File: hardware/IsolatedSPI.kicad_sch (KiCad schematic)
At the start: 9 parts, among them IC6 LTC6820IMS

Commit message: schematic done
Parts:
- removed D5: ESDA5V3SC5, Package_TO_SOT_SMD:SOT-23-6, symbol Power_Protection:ESDA5V3SC5
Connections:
- no-connect marks 2 -> 0
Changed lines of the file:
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@@
 	(paper "A4")
-	(junction
-		(at 170.18 83.82)
-		(diameter 0)
-		(color 0 0 0 0)
-	)
 	(junction
 		(at 95.25 111.76)
@@
 	)
 	(junction
-		(at 172.72 86.36)
-		(diameter 0)
-		(color 0 0 0 0)
-	)
-	(junction
 		(at 85.09 86.36)
 		(diameter 0)
@@
 		(color 0 0 0 0)
 	)
-	(no_connect
-		(at 175.26 81.28)
-	)
-	(no_connect
-		(at 167.64 81.28)
-	)
 	(wire
 		(pts
@@
 	(wire
 		(pts
-			(xy 120.65 86.36) (xy 172.72 86.36)
+			(xy 120.65 86.36) (xy 194.31 86.36)
 		)
 		(stroke
@@
 	(wire
 		(pts
-			(xy 172.72 81.28) (xy 172.72 86.36)
-		)
-		(stroke
-			(width 0)
-			(type default)
-		)
-	)
-	(wire
-		(pts
 			(xy 194.31 83.82) (xy 194.31 81.28)
 		)
@@
 	(wire
 		(pts
-			(xy 172.72 68.58) (xy 172.72 71.12)
-		)
-		(stroke
-			(width 0)
-			(type default)
-		)
-	)
-	(wire
-		(pts
 			(xy 129.54 116.84) (xy 120.65 116.84)
 		)
@@
 	(wire
 		(pts
-			(xy 170.18 83.82) (xy 194.31 83.82)
-		)
-		(stroke
-			(width 0)
-			(type default)
-		)
-	)
-	(wire
-		(pts
 			(xy 92.71 86.36) (xy 95.25 86.36)
 		)
@@
 	(wire
 		(pts
-			(xy 170.18 81.28) (xy 170.18 83.82)
-		)
-		(stroke
-			(width 0)
-			(type default)
-		)
-	)
-	(wire
-		(pts
 			(xy 85.09 86.36) (xy 87.63 86.36)
 		)
@@
 	(wire
 		(pts
-			(xy 172.72 86.36) (xy 194.31 86.36)
-		)
-		(stroke
-			(width 0)
-			(type default)
-		)
-	)
-	(wire
-		(pts
 			(xy 203.2 81.28) (xy 203.2 82.55)
 		)
@@
 	(wire
 		(pts
-			(xy 120.65 83.82) (xy 170.18 83.82)
+			(xy 120.65 83.82) (xy 194.31 83.82)
 		)
 		(stroke
@@
 					(unit 1)
 				)
-			)
-		)
-	)
-	(symbol
-		(lib_name "GND_31")
-		(lib_id "power:GND")
-		(at 172.72 68.58 180)
-		(unit 1)
-		(exclude_from_sim no)
-		(in_bom yes)
-		(on_board yes)
-		(dnp no)
-		(property "Reference" "#PWR099"
-			(at 172.72 62.23 0)
-			(effects
-				(font
-					(size 1.27 1.27)
-				)
-				(hide yes)
-			)
-		)
-		(property "Value" "GNDISO"
-			(at 172.593 64.1858 0)
-			(effects
-				(font
-					(size 1.27 1.27)
-				)
-			)
-		)
-		(property "Footprint" ""
-			(at 172.72 68.58 0)
-			(effects
-				(font
-					(size 1.27 1.27)
-				)
-				(hide yes)
-			)
-		)
-		(property "Datasheet" ""
-			(at 172.72 68.58 0)
-			(effects
-				(font
-					(size 1.27 1.27)
-				)
-				(hide yes)
-			)
-		)
-		(property "Description" ""
-			(at 172.72 68.58 0)
-			(effects
-				(font
-					(size 1.27 1.27)
-				)
-				(hide yes)
-			)
-		)
-		(pin "1"
-		)
-		(instances
-			(project "PUTM_EV_BMS_HV_MASTER_2023"
-				(path "/b456cffc-d9d7-4c91-91f2-36ec9a65dd1b/6b45fd0b-238d-49b3-829e-372c6baba47f"
-					(reference "#PWR099")
-					(unit 1)
-				)
-			)
-		)
-	)
-	(symbol
-		(lib_name "ESDA5V3SC5_3")
-		(lib_id "Power_Protection:ESDA5V3SC5")
-		(at 172.72 76.2 180)
-		(unit 1)
-		(exclude_from_sim no)
-		(in_bom yes)
-		(on_board yes)
-		(dnp no)
-		(property "Reference" "D5"
-			(at 179.07 74.93 0)
-			(effects
-				(font
-					(size 1.27 1.27)
-				)
-				(justify right)
-			)
-		)
-		(property "Value" "ESDA5V3SC5"
-			(at 179.07 77.47 0)
-			(effects
-				(font
-					(size 1.27 1.27)
-				)
-				(justify right)
-			)
-		)
-		(property "Footprint" "Package_TO_SOT_SMD:SOT-23-6"
-			(at 165.1 74.93 0)
-			(effects
-				(font
-					(size 1.27 1.27)
-				)
-				(justify left)
-				(hide yes)
-			)
-		)
-		(property "Datasheet" "https://www.mouser.pl/datasheet/2/389/cd00002055-1795703.pdf"
-			(at 169.545 79.375 0)
-			(effects
-				(font
-					(size 1.27 1.27)
-				)
-				(hide yes)
-			)
-		)
-		(property "Description" "Quad TVS Diode Array, 5.3V Standoff, 4 Channels, 400W, ±30kV, SOT-23-5"
-			(at 172.72 76.2 0)
-			(effects
-				(font
-					(size 1.27 1.27)
-				)
-				(hide yes)
-			)
-		)
-		(property "Manufacturer_Part_Number" "ESDA5V3SC5"
-			(at 172.72 76.2 0)
-			(effects
-				(font
-					(size 1.27 1.27)
-				)
-				(hide yes)
-			)
-		)
-		(property "Mouser Part Number" "511-ESDA5V3SC5"
-			(at 172.72 76.2 0)
-			(effects
-				(font
-					(size 1.27 1.27)
-				)
-				(hide yes)
-			)
-		)
-		(property "Mouser Price/Stock" "https://www.mouser.pl/ProductDetail/STMicroelectronics/ESDA5V3SC5?qs=vqk%252BPKT8fSw1EexaRsSoaw%3D%3D"
-			(at 172.72 76.2 0)
-			(effects
-				(font
-					(size 1.27 1.27)
-				)
-				(hide yes)
-			)
-		)
-		(pin "2"
-		)
-		(pin "3"
-		)
-		(pin "1"
-		)
-		(pin "4"
-		)
-		(pin "5"
-		)
-		(pin "6"
-		)
-		(instances
-			(project "PUTM_EV_BMS_HV_MASTER_2023"
-				(path "/b456cffc-d9d7-4c91-91f2-36ec9a65dd1b/6b45fd0b-238d-49b3-829e-372c6baba47f"
-					(reference "D5")
-					(unit 1)
-				)

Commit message: mama comit
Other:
- moved on the sheet: C43, C50, R20
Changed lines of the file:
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@@
 	)
 	(junction
-		(at 203.2 88.9)
+		(at 191.77 88.9)
 		(diameter 0)
 		(color 0 0 0 0)
@@
 	)
 	(junction
-		(at 203.2 81.28)
+		(at 191.77 81.28)
 		(diameter 0)
 		(color 0 0 0 0)
@@
 	(wire
 		(pts
-			(xy 203.2 81.28) (xy 205.74 81.28)
-		)
-		(stroke
-			(width 0)
-			(type default)
-		)
-	)
-	(wire
-		(pts
-			(xy 120.65 86.36) (xy 194.31 86.36)
+			(xy 191.77 81.28) (xy 194.31 81.28)
+		)
+		(stroke
+			(width 0)
+			(type default)
+		)
+	)
+	(wire
+		(pts
+			(xy 120.65 86.36) (xy 182.88 86.36)
 		)
 		(stroke
@@
 	(wire
 		(pts
-			(xy 213.36 83.82) (xy 219.71 83.82)
+			(xy 201.93 83.82) (xy 208.28 83.82)
 		)
 		(stroke
@@
 	(wire
 		(pts
-			(xy 194.31 83.82) (xy 194.31 81.28)
+			(xy 182.88 83.82) (xy 182.88 81.28)
 		)
 		(stroke
@@
 	(wire
 		(pts
-			(xy 203.2 88.9) (xy 205.74 88.9)
+			(xy 191.77 88.9) (xy 194.31 88.9)
 		)
 		(stroke
@@
 	(wire
 		(pts
-			(xy 210.82 81.28) (xy 213.36 81.28)
+			(xy 199.39 81.28) (xy 201.93 81.28)
 		)
 		(stroke
@@
 	(wire
 		(pts
-			(xy 203.2 87.63) (xy 203.2 88.9)
+			(xy 191.77 87.63) (xy 191.77 88.9)
 		)
 		(stroke
@@
 	(wire
 		(pts
-			(xy 210.82 88.9) (xy 213.36 88.9)
-		)
-		(stroke
-			(width 0)
-			(type default)
-		)
-	)
-	(wire
-		(pts
-			(xy 213.36 88.9) (xy 213.36 86.36)
+			(xy 199.39 88.9) (xy 201.93 88.9)
+		)
+		(stroke
+			(width 0)
+			(type default)
+		)
+	)
+	(wire
+		(pts
+			(xy 201.93 88.9) (xy 201.93 86.36)
 		)
 		(stroke
@@
 	(wire
 		(pts
-			(xy 203.2 81.28) (xy 203.2 82.55)
+			(xy 191.77 81.28) (xy 191.77 82.55)
 		)
 		(stroke
@@
 	(wire
 		(pts
-			(xy 194.31 88.9) (xy 203.2 88.9)
-		)
-		(stroke
-			(width 0)
-			(type default)
-		)
-	)
-	(wire
-		(pts
-			(xy 194.31 81.28) (xy 203.2 81.28)
+			(xy 182.88 88.9) (xy 191.77 88.9)
+		)
+		(stroke
+			(width 0)
+			(type default)
+		)
+	)
+	(wire
+		(pts
+			(xy 182.88 81.28) (xy 191.77 81.28)
 		)
 		(stroke
@@
 	(wire
 		(pts
-			(xy 120.65 83.82) (xy 194.31 83.82)
-		)
-		(stroke
-			(width 0)
-			(type default)
-		)
-	)
-	(wire
-		(pts
-			(xy 213.36 86.36) (xy 219.71 86.36)
-		)
-		(stroke
-			(width 0)
-			(type default)
-		)
-	)
-	(wire
-		(pts
-			(xy 213.36 83.82) (xy 213.36 81.28)
+			(xy 120.65 83.82) (xy 182.88 83.82)
+		)
+		(stroke
+			(width 0)
+			(type default)
+		)
+	)
+	(wire
+		(pts
+			(xy 201.93 86.36) (xy 208.28 86.36)
+		)
+		(stroke
+			(width 0)
+			(type default)
+		)
+	)
+	(wire
+		(pts
+			(xy 201.93 83.82) (xy 201.93 81.28)
 		)
 		(stroke
@@
 	(wire
 		(pts
-			(xy 194.31 86.36) (xy 194.31 88.9)
+			(xy 182.88 86.36) (xy 182.88 88.9)
 		)
 		(stroke
@@
 	(hierarchical_label "OUT+"
 		(shape input)
-		(at 219.71 83.82 0)
+		(at 208.28 83.82 0)
 		(fields_autoplaced yes)
 		(effects
@@
 	(hierarchical_label "OUT-"
 		(shape input)
-		(at 219.71 86.36 0)
+		(at 208.28 86.36 0)
 		(fields_autoplaced yes)
 		(effects
@@
 	(symbol
 		(lib_id "c2824c562jggacauto:C2824C562JGGACAUTO")
-		(at 208.28 81.28 0)
+		(at 196.85 81.28 0)
 		(unit 1)
 		(exclude_from_sim no)
@@
 		(dnp no)
 		(property "Reference" "C43"
-			(at 208.28 74.93 0)
+			(at 196.85 74.93 0)
 			(effects
 				(font
@@
 		)
 		(property "Value" "10nF/1kV"
-			(at 208.28 77.47 0)
+			(at 196.85 77.47 0)
 			(effects
 				(font
@@
 		)
 		(property "Footprint" "Capacitor_SMD:C_1206_3216Metric"
-			(at 217.17 80.01 0)
+			(at 205.74 80.01 0)
 			(effects
 				(font
@@
 		)
 		(property "Datasheet" "https://content.kemet.com/datasheets/KEM_C1080_C0G_HV_AUTO_SMD.pdf"
-			(at 217.17 82.55 0)
+			(at 205.74 82.55 0)
 			(effects
 				(font
@@
 		)
 		(property "Description" "SMD Auto C0G HV, Ceramic, 5600 pF, 5%, 2000 VDC, 2400 VDC, 125C, -55C, C0G, SMD, MLCC, Ultra-Stable, Low Loss, High Voltage, Automotive Grade, 0.1 % , 100 GOhms, 540 mg, 2824, 7.1mm, 6.1mm, 2.5mm, 1.27mm, 300, 78  Weeks, 120"
-			(at 217.17 85.09 0)
+			(at 205.74 85.09 0)
 			(effects
 				(font
@@
 		)
 		(property "Height" ""
-			(at 217.17 87.63 0)
+			(at 205.74 87.63 0)
 			(effects
 				(font
@@
 		)
 		(property "Mouser Part Number" "80-C2824C562JGGAUTO"
-			(at 217.17 90.17 0)
+			(at 205.74 90.17 0)
 			(effects
 				(font
@@
 		)
 		(property "Mouser Price/Stock" "https://www.mouser.co.uk/ProductDetail/KEMET/C2824C562JGGACAUTO?qs=5aG0NVq1C4xKMWO6DzsxHA%3D%3D"
-			(at 217.17 92.71 0)
+			(at 205.74 92.71 0)
 			(effects
 				(font
@@
 		)
 		(property "Manufacturer_Name" ""
-			(at 217.17 95.25 0)
+			(at 205.74 95.25 0)
 			(effects
 				(font
@@
 		)
 		(property "Manufacturer_Part_Number" "C2824C562JGGACAUTO"
-			(at 217.17 97.79 0)
+			(at 205.74 97.79 0)
 			(effects
 				(font
@@
 		)
 		(property "Arrow Part Number" ""
-			(at 208.28 81.28 0)
+			(at 196.85 81.28 0)
 			(effects
 				(font
@@
 		)
 		(property "Arrow Price/Stock" ""
-			(at 208.28 81.28 0)
+			(at 196.85 81.28 0)
 			(effects
 				(font
@@
 		)
 		(property "Mouser Url" ""
-			(at 208.28 81.28 0)
+			(at 196.85 81.28 0)
 			(effects
 				(font
@@
 	(symbol
 		(lib_id "c2824c562jggacauto:C2824C562JGGACAUTO")
-		(at 208.28 88.9 0)
+		(at 196.85 88.9 0)
 		(unit 1)
 		(exclude_from_sim no)
@@
 		(dnp no)
 		(property "Reference" "C50"
-			(at 208.28 92.71 0)
+			(at 196.85 92.71 0)
 			(effects
 				(font
@@
 		)
 		(property "Value" "10nF/1kV"
-			(at 208.28 95.25 0)
+			(at 196.85 95.25 0)
 			(effects
 				(font
@@
 		)
 		(property "Footprint" "Capacitor_SMD:C_1206_3216Metric"
-			(at 217.17 87.63 0)
+			(at 205.74 87.63 0)
 			(effects
 				(font
@@
 		)
 		(property "Datasheet" "https://content.kemet.com/datasheets/KEM_C1080_C0G_HV_AUTO_SMD.pdf"
-			(at 217.17 90.17 0)
+			(at 205.74 90.17 0)
 			(effects
 				(font
@@
 		)
 		(property "Description" "SMD Auto C0G HV, Ceramic, 5600 pF, 5%, 2000 VDC, 2400 VDC, 125C, -55C, C0G, SMD, MLCC, Ultra-Stable, Low Loss, High Voltage, Automotive Grade, 0.1 % , 100 GOhms, 540 mg, 2824, 7.1mm, 6.1mm, 2.5mm, 1.27mm, 300, 78  Weeks, 120"
-			(at 217.17 92.71 0)
+			(at 205.74 92.71 0)
 			(effects
 				(font
@@
 		)
 		(property "Height" ""
-			(at 217.17 95.25 0)
+			(at 205.74 95.25 0)
 			(effects
 				(font
@@
 		)
 		(property "Mouser Part Number" "80-C2824C562JGGAUTO"
-			(at 217.17 97.79 0)
+			(at 205.74 97.79 0)
 			(effects
 				(font
@@
 		)
 		(property "Mouser Price/Stock" "https://www.mouser.co.uk/ProductDetail/KEMET/C2824C562JGGACAUTO?qs=5aG0NVq1C4xKMWO6DzsxHA%3D%3D"
-			(at 217.17 100.33 0)
+			(at 205.74 100.33 0)
 			(effects
 				(font
@@
 		)
 		(property "Manufacturer_Name" ""
-			(at 217.17 102.87 0)
+			(at 205.74 102.87 0)
 			(effects
 				(font
@@
 		)
 		(property "Manufacturer_Part_Number" "C2824C562JGGACAUTO"
-			(at 217.17 105.41 0)
+			(at 205.74 105.41 0)
 			(effects
 				(font
@@
 		)
 		(property "Arrow Part Number" ""
-			(at 208.28 88.9 0)
+			(at 196.85 88.9 0)
 			(effects
 				(font
@@
 		)
 		(property "Arrow Price/Stock" ""
-			(at 208.28 88.9 0)
+			(at 196.85 88.9 0)
 			(effects
 				(font
@@
 		)
 		(property "Mouser Url" ""
-			(at 208.28 88.9 0)
+			(at 196.85 88.9 0)
 			(effects
 				(font
@@
 	(symbol
 		(lib_id "Device:R_Small")
-		(at 203.2 85.09 0)
+		(at 191.77 85.09 0)
 		(mirror y)
 		(unit 1)
@@
 		(dnp no)
 		(property "Reference" "R20"
-			(at 201.93 83.82 0)
+			(at 190.5 83.82 0)
 			(effects
 				(font
@@
 		)
 		(property "Value" "120"
-			(at 201.93 86.36 0)
+			(at 190.5 86.36 0)
 			(effects
 				(font
@@
 		)
 		(property "Footprint" "Resistor_SMD:R_0603_1608Metric"
-			(at 203.2 85.09 0)
+			(at 191.77 85.09 0)
 			(effects
 				(font
@@
 		)
 		(property "Datasheet" "~"
-			(at 203.2 85.09 0)
+			(at 191.77 85.09 0)
 			(effects
 				(font
@@
 		)
 		(property "Description" ""
-			(at 203.2 85.09 0)
+			(at 191.77 85.09 0)
 			(effects
 				(font
@@
 		)
 		(property "Manufacturer_Name" "--"
-			(at 203.2 85.09 0)
+			(at 191.77 85.09 0)
 			(effects
 				(font
@@
 		)
 		(property "Manufacturer_Part_Number" "--"
-			(at 203.2 85.09 0)
+			(at 191.77 85.09 0)
 			(effects
 				(font
@@
 		)
 		(property "Arrow Part Number" ""
-			(at 203.2 85.09 0)
+			(at 191.77 85.09 0)
 			(effects
 				(font
@@
 		)
 		(property "Arrow Price/Stock" ""
-			(at 203.2 85.09 0)
+			(at 191.77 85.09 0)
 			(effects
 				(font
@@
 		)
 		(property "Mouser Url" ""
-			(at 203.2 85.09 0)
-			(effects
-				(font
+			(at 191.77 85.09 0)
+			(effects
+				(font

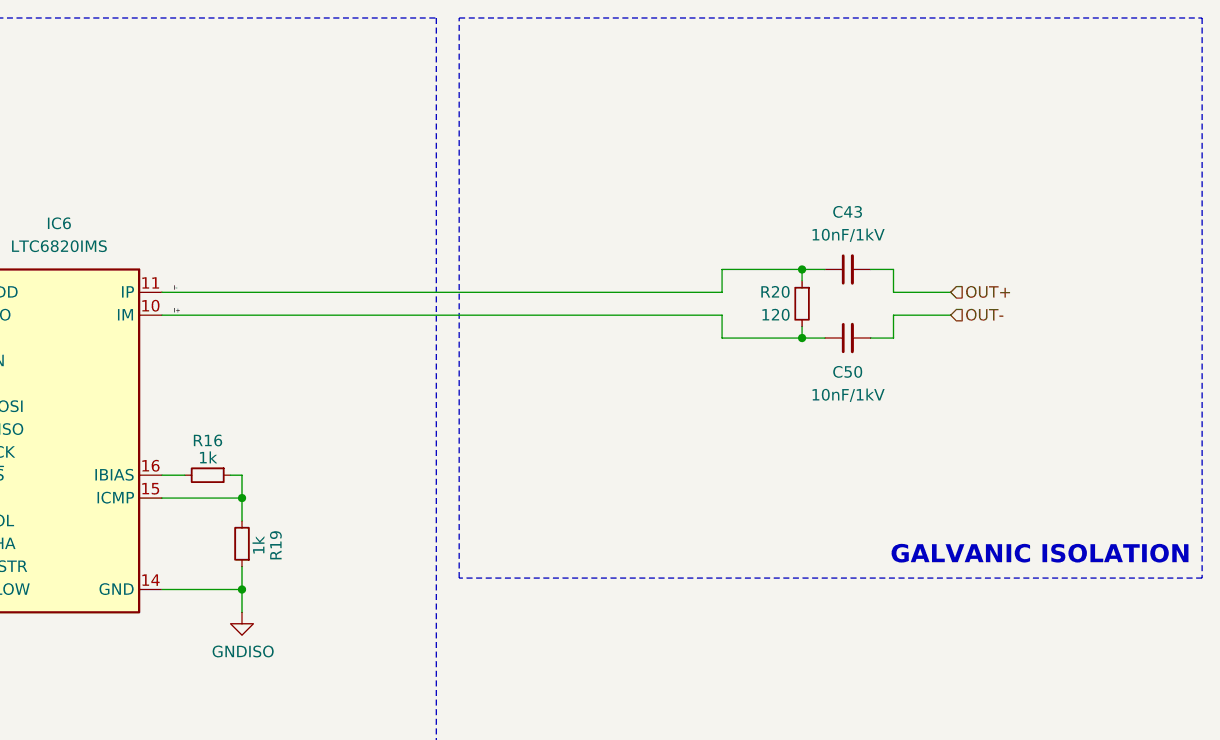
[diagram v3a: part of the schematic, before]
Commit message: inductors 3d models fix, smaller relay (same series as the one from IMD), other + sync
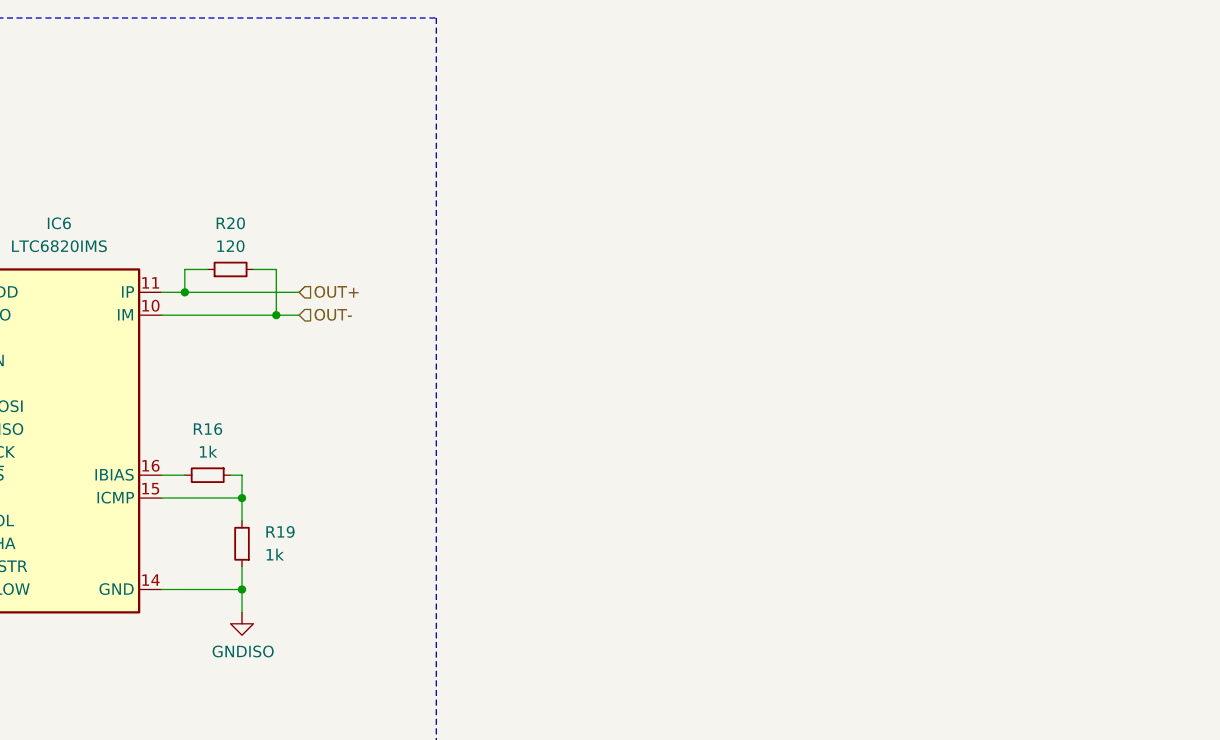
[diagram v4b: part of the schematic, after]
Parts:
- removed C43, C50: 10nF/1kV, Capacitor_SMD:C_1206_3216Metric, symbol c2824c562jggacauto:C2824C562JGGACAUTO
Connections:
- net I+ is gone; now on net OUT-: IC6.10 (IM), R20.2
- net I- is gone; now on net OUT+: IC6.11 (IP), R20.1
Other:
- note removed: "GALVANIC ISOLATION"
- moved on the sheet: R20

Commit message: sync
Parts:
- added C43: 220nF, Capacitor_SMD:C_0603_1608Metric, symbol Device:C_Small
- added C53, C78: 100nF, Capacitor_SMD:C_0603_1608Metric, symbol Device:C_Small
- added C79, C80: 100p, Capacitor_SMD:C_0603_1608Metric, symbol Device:C_Small
- added IC3: BQ79600PWRQ1, Package_SO:TSSOP-16_4.4x5mm_P0.65mm, symbol Samacsys_kicad_sym:BQ79600PWRQ1
- added R94: 10k, Resistor_SMD:R_0603_1608Metric, symbol Device:R_Small
- added R95, R99: 100k, Resistor_SMD:R_0603_1608Metric, symbol Device:R_Small
- added R96, R98: 51, Resistor_SMD:R_0603_1608Metric, symbol Device:R_Small
- added R97: 1k, Resistor_SMD:R_0603_1608Metric, symbol Device:R_Small
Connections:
- net +3.3VISO: now also C78.1, IC3.3 (VIO), R94.1, R95.1, R99.1
- net GNDISO: now also C43.1, C53.2, C78.2, C79.1, C80.1, IC3.9 (GND)
- net MISO: now also IC3.5 (MISO/TX), R94.2
- net MOSI: now also IC3.4 (MOSI/RX)
- net OUT+: now also R96.1
- net OUT-: now also R98.1
- net SCK: now also IC3.6 (SCLK)
- net ~{CS}: now also IC3.7 (NCS)
- new net: C79.2, IC3.13 (COMHP), R96.2, R97.2
- new net: C80.2, IC3.12 (COMHN), R97.1, R98.2
- new net: C53.1, IC3.1 (DVDD)
- new net +5VISO: C43.2, IC3.14 (CVDD), IC3.15 (BAT), IC3.16 (INH)
- new net SPI_RDY: IC3.8 (SPI_RDY), R95.2
- new net ~{FLT}: IC3.2 (NFAULT), R99.2
- no-connect marks 0 -> 2
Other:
- note added: "BQ79600 ISO INTERFACE"
- note added: "SPI PULLUP"

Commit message: sync
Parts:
- C18, C42, C53, C78: Mouser Price/Stock (none) -> https://www.mouser.pl/ProductDetail/KEMET/C0603C104J3RACTU?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
- IC6: Mouser Part Number (none) -> LTC6820IMS#PBF; Mouser Price/Stock (none) -> https://www.mouser.pl/ProductDetail/Analog-Devices/LTC6820I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
- R94, R95, R99: Mouser Price/Stock (none) -> https://www.mouser.pl/ProductDetail/YAGEO/RT0603DRE07100KL?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

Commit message: the connectors wil stay and wont be changed further
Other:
- moved on the sheet: C18, C42, C43, C53, C78, C79, C80, IC3, IC6, R16, R19, R20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
